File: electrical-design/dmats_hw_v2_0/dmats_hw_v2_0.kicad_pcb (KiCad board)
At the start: 2 copper layers, 132.7 x 132.7 mm, 29 parts, among them Q1 PSMN1R0-30YLC,115, Q2 PSMN1R0-30YLC,115, Q3 PSMN1R0-30YLC,115, Q4 PSMN1R0-30YLC,115, SW2 Motor_2BitEncoder, U2 A1324, U3 A1324, U4 ABX00042

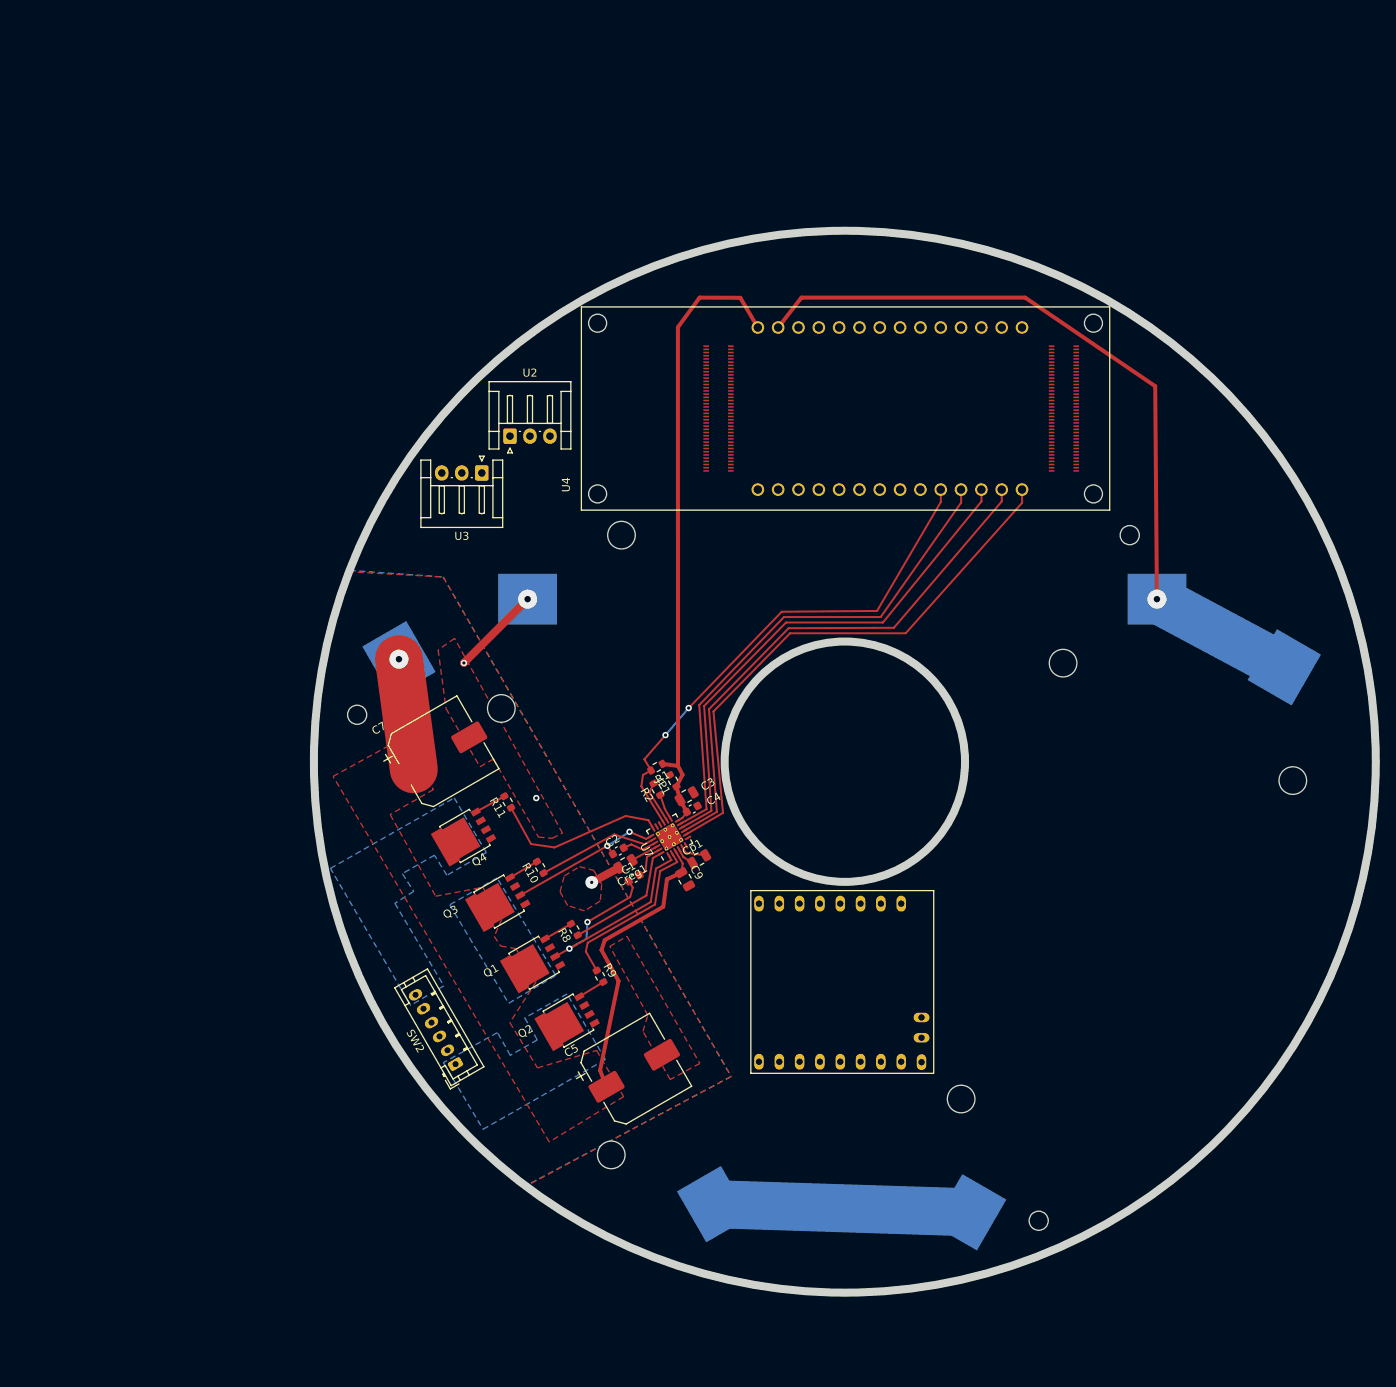
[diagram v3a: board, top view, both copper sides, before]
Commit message: sim updates for force analysis and visual clean up on elec drawings
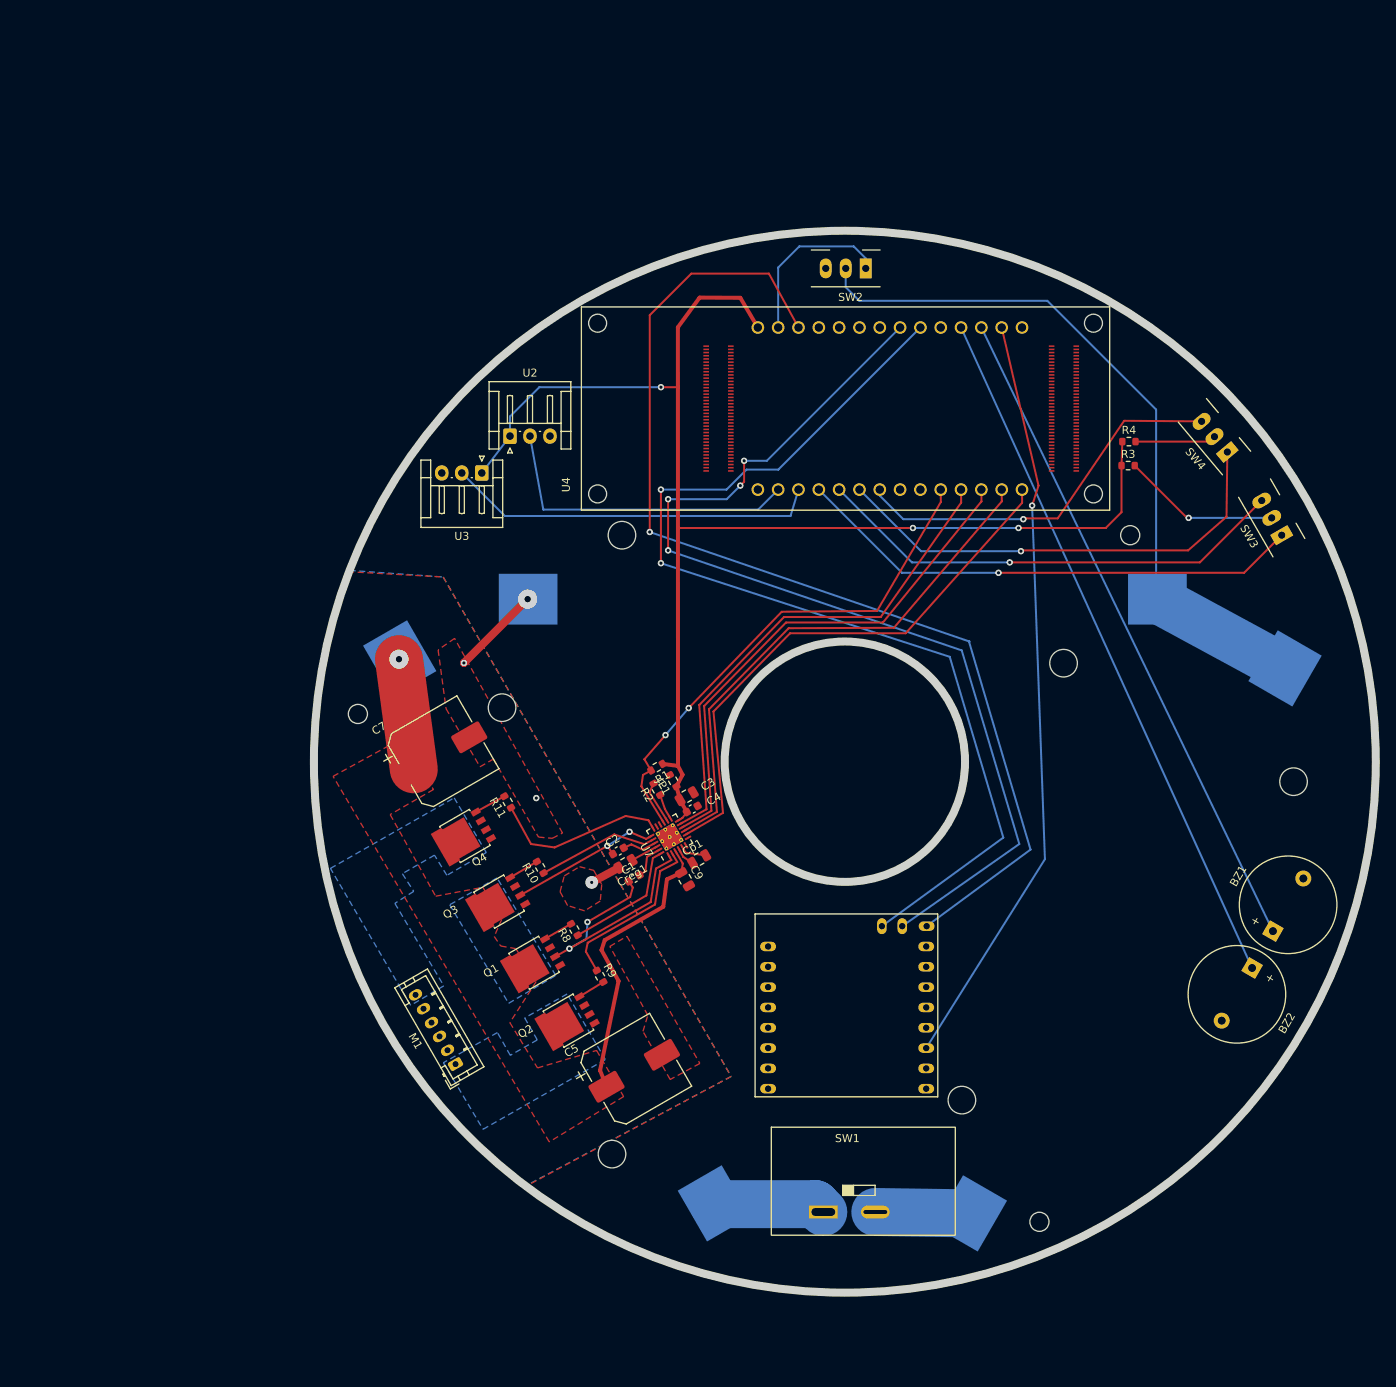
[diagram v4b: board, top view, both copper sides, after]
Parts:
- added BZ1: Buzzer, Buzzer_Beeper:Buzzer_12x9.5RM7.6, F.Cu at (213.9, 168.1)
- added BZ2: Buzzer, Buzzer_Beeper:Buzzer_12x9.5RM7.6, F.Cu at (211.3, 172.7)
- added R3: 10k, Resistor_SMD:R_0603_1608Metric, F.Cu at (195.8, 109.9)
- added R4: 10k, Resistor_SMD:R_0603_1608Metric, F.Cu at (195.9, 106.9)
- added SW1: SW_SPST, DMATS_capstone:SW_DIP_SPSTx01_Slide_Power, F.Cu at (151.3, 206.0)
- added SW2: SW_SPDT, DMATS_capstone:CUI_SLW-913535-2A-RA-D_SPDT_Angled, F.Cu at (162.5, 85.2)
- added SW3: SW_SPDT, DMATS_capstone:CUI_SLW-913535-2A-RA-D_SPDT_Angled, F.Cu at (214.8, 118.2)
- added SW4: SW_SPDT, DMATS_capstone:CUI_SLW-913535-2A-RA-D_SPDT_Angled, F.Cu at (207.9, 107.8)
- moved BT2 71.4 mm to (195.8, 169.3), turned to 60 degrees
- moved BT1 71.3 mm to (124.4, 168.1), turned to -60 degrees
- moved U1 8.44 mm to (166.8, 178.9), turned to 90 degrees
- moved BT3 0.06 mm to (160.1, 126.6)
- renumbered SW2 to M1
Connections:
- BT1 pad 1: Net-(BT1-+) -> +BATT
- BT1 pad 2: /VIN -> Net-(BT1--)
- BT2 pad 1: +BATT -> Net-(BT2-+)
- BT2 pad 2: Net-(BT1-+) -> Net-(BT2--)
- BT3 pad 1: /VIN -> Net-(BT2--)
- U4 pad JA4: unconnected-(U4C-A2_D17-PadJA4) -> /SW_A
- U4 pad JA5: unconnected-(U4C-A3_D18-PadJA5) -> /SW_B
- U4 pad JA6: unconnected-(U4C-A4_D19-PadJA6) -> /SW_C
- U4 pad JA7: unconnected-(U4C-A5_D20-PadJA7) -> /SW_D
- U4 pad JD11: unconnected-(U4C-D9-PadJD11) -> /BZ_B
- U4 pad JD12: unconnected-(U4C-D8-PadJD12) -> /BZ_A
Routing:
- net +3.3V: track 0.00 -> 137.4 mm, vias 0 -> 1
- net /I2C-SDA: track 0.00 -> 130.4 mm, vias 0 -> 2
- net /I2C-SCL: track 0.00 -> 127.8 mm, vias 0 -> 4
- net +5V: track 78.7 -> 174.6 mm, vias 0 -> 3
- net /GPIO_CS: track 0.00 -> 95.0 mm, vias 0 -> 1
- net Net-(BT2--): track 0.00 -> 89.4 mm
- net /BZ_B: track 0.00 -> 87.9 mm
- net /BZ_A: track 0.00 -> 83.8 mm
- net /VIN: track 97.1 -> 21.4 mm, vias 1 -> 0
- net /SW_A: track 0.00 -> 64.1 mm, vias 0 -> 1
- net /SW_B: track 0.00 -> 59.8 mm, vias 0 -> 1
- net /SW_C: track 0.00 -> 58.8 mm, vias 0 -> 1
- net /SW_D: track 0.00 -> 49.0 mm, vias 0 -> 1
- net /HES_OUT2: track 0.00 -> 46.8 mm
- net /HES_OUT1: track 0.00 -> 39.7 mm
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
